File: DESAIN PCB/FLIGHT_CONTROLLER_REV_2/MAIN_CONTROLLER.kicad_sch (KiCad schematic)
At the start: 31 parts, among them J1 AVR-ISP-10, J2 USB B, J3 Conn_01x03_Male, J4 Conn_01x03_Male, J5 Conn_01x03_Male, J6 Conn_01x03_Male, J7 Conn_01x08_Female, J8 Conn_01x08_Female, SW1 SW_SPST, U1 ATmega328P-P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

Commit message: add PCB REV 2
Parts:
- added J12: TRANSMITTER_1, Connector_PinHeader_2.54mm:PinHeader_1x04_P2.54mm_Vertical, symbol Connector:Conn_01x04_Male
- added J13: TRANSMITTER_2, Connector_PinHeader_2.54mm:PinHeader_1x04_P2.54mm_Vertical, symbol Connector:Conn_01x04_Male
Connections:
- net MOSI is gone; now on net D11: J1.1 (MOSI), U1.17 (PB3)
- net +5V: now also J12.1 (Pin_1), J13.1 (Pin_1)
- net GND: now also J12.4 (Pin_4), J13.4 (Pin_4)
- net RX: now also J12.2 (Pin_2), J13.2 (Pin_2)
- net TX: now also J12.3 (Pin_3), J13.3 (Pin_3)
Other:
- note removed: "==> D11"
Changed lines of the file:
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@@
+    (stroke (width 0) (type default) (color 0 0 0 0))
+  )
+  (wire (pts (xy 132.08 127) (xy 137.16 127))
     (stroke (width 0) (type default) (color 0 0 0 0))
   )
@@
     (stroke (width 0) (type default) (color 0 0 0 0))
   )
+  (wire (pts (xy 152.4 127) (xy 157.48 127))
+    (stroke (width 0) (type default) (color 0 0 0 0))
+  )
   (polyline (pts (xy 153.67 101.092) (xy 153.67 112.776))
     (stroke (width 0) (type default) (color 0 0 0 0))
@@
     (stroke (width 0) (type default) (color 0 0 0 0))
   )
+  (wire (pts (xy 132.08 124.46) (xy 137.16 124.46))
+    (stroke (width 0) (type default) (color 0 0 0 0))
+  )
   (polyline (pts (xy 129.54 36.195) (xy 129.54 48.26))
     (stroke (width 0) (type default) (color 0 0 0 0))
@@
     (stroke (width 0) (type default) (color 0 0 0 0))
   )
+  (wire (pts (xy 56.896 43.18) (xy 74.93 43.18))
+    (stroke (width 0) (type default) (color 0 0 0 0))
+  )
   (polyline (pts (xy 18.542 113.792) (xy 18.542 115.062))
     (stroke (width 0) (type default) (color 0 0 0 0))
@@
     (stroke (width 0) (type default) (color 0 0 0 0))
   )
-  (wire (pts (xy 56.896 43.18) (xy 65.786 43.18))
-    (stroke (width 0) (type default) (color 0 0 0 0))
-  )
   (polyline (pts (xy 205.994 85.344) (xy 205.994 88.138))
     (stroke (width 0) (type default) (color 0 0 0 0))
   )
   (wire (pts (xy 130.81 34.925) (xy 130.81 44.958))
+    (stroke (width 0) (type default) (color 0 0 0 0))
+  )
+  (wire (pts (xy 152.4 124.46) (xy 157.48 124.46))
     (stroke (width 0) (type default) (color 0 0 0 0))
   )
@@
     (effects (font (size 1.27 1.27) (thickness 0.254) bold) (justify left bottom))
   )
-  (text "==> D11" (at 65.786 43.18 0)
-    (effects (font (size 1.27 1.27)) (justify left bottom))
-  )
   (text "IMU GY 88-A" (at 209.804 89.408 0)
     (effects (font (size 1.27 1.27) bold) (justify left bottom))
@@
     (effects (font (size 1.27 1.27)) (justify right bottom))
   )
+  (label "RX" (at 137.16 124.46 180)
+    (effects (font (size 1.27 1.27)) (justify right bottom))
+  )
   (label "D4" (at 65.786 88.9 180)
     (effects (font (size 1.27 1.27)) (justify right bottom))
@@
   )
   (label "D7" (at 174.498 108.204 180)
+    (effects (font (size 1.27 1.27)) (justify right bottom))
+  )
+  (label "TX" (at 157.48 127 180)
     (effects (font (size 1.27 1.27)) (justify right bottom))
   )
@@
     (effects (font (size 1.27 1.27)) (justify right bottom))
   )
+  (label "TX" (at 137.16 127 180)
+    (effects (font (size 1.27 1.27)) (justify right bottom))
+  )
   (label "D9" (at 149.098 98.044 180)
     (effects (font (size 1.27 1.27)) (justify right bottom))
@@
   )
   (label "D4" (at 174.498 100.584 180)
+    (effects (font (size 1.27 1.27)) (justify right bottom))
+  )
+  (label "RX" (at 157.48 124.46 180)
+    (effects (font (size 1.27 1.27)) (justify right bottom))
+  )
+  (label "D11" (at 74.93 43.18 180)
     (effects (font (size 1.27 1.27)) (justify right bottom))
   )
@@
     (pin "3")
   )
+  (symbol (lib_id "power:GND") (at 152.4 129.54 90) (unit 1)
+    (in_bom yes) (on_board yes) (fields_autoplaced)
+    (property "Reference" "#PWR0108" (id 0) (at 158.75 129.54 0)
+      (effects (font (size 1.27 1.27)) hide)
+    )
+    (property "Value" "GND" (id 1) (at 156.21 129.5399 90)
+      (effects (font (size 1.27 1.27)) (justify right))
+    )
+    (property "Footprint" "" (id 2) (at 152.4 129.54 0)
+      (effects (font (size 1.27 1.27)) hide)
+    )
+    (property "Datasheet" "" (id 3) (at 152.4 129.54 0)
+      (effects (font (size 1.27 1.27)) hide)
+    )
+    (pin "1")
+  )
   (symbol (lib_id "Device:C_Small") (at 94.742 45.974 270) (mirror x) (unit 1)
     (in_bom yes) (on_board yes)
@@
     (pin "8")
     (pin "9")
+  )
+  (symbol (lib_id "power:GND") (at 132.08 129.54 90) (unit 1)
+    (in_bom yes) (on_board yes) (fields_autoplaced)
+    (property "Reference" "#PWR0105" (id 0) (at 138.43 129.54 0)
+      (effects (font (size 1.27 1.27)) hide)
+    )
+    (property "Value" "GND" (id 1) (at 135.89 129.5399 90)
+      (effects (font (size 1.27 1.27)) (justify right))
+    )
+    (property "Footprint" "" (id 2) (at 132.08 129.54 0)
+      (effects (font (size 1.27 1.27)) hide)
+    )
+    (property "Datasheet" "" (id 3) (at 132.08 129.54 0)
+      (effects (font (size 1.27 1.27)) hide)
+    )
+    (pin "1")
   )
   (symbol (lib_id "Connector:Conn_01x03_Male") (at 141.224 94.996 0) (unit 1)
@@
     (pin "2")
   )
+  (symbol (lib_id "power:+5V") (at 152.4 121.92 270) (unit 1)
+    (in_bom yes) (on_board yes) (fields_autoplaced)
+    (property "Reference" "#PWR0107" (id 0) (at 148.59 121.92 0)
+      (effects (font (size 1.27 1.27)) hide)
+    )
+    (property "Value" "+5V" (id 1) (at 156.21 121.9199 90)
+      (effects (font (size 1.27 1.27)) (justify left))
+    )
+    (property "Footprint" "" (id 2) (at 152.4 121.92 0)
+      (effects (font (size 1.27 1.27)) hide)
+    )
+    (property "Datasheet" "" (id 3) (at 152.4 121.92 0)
+      (effects (font (size 1.27 1.27)) hide)
+    )
+    (pin "1")
+  )
   (symbol (lib_id "power:+5V") (at 131.064 94.996 270) (unit 1)
     (in_bom yes) (on_board yes)
@@
     (pin "2")
   )
+  (symbol (lib_id "Connector:Conn_01x04_Male") (at 147.32 124.46 0) (unit 1)
+    (in_bom yes) (on_board yes) (fields_autoplaced)
+    (property "Reference" "J13" (id 0) (at 147.955 116.84 0))
+    (property "Value" "TRANSMITTER_2" (id 1) (at 147.955 119.38 0))
+    (property "Footprint" "Connector_PinHeader_2.54mm:PinHeader_1x04_P2.54mm_Vertical" (id 2) (at 147.32 124.46 0)
+      (effects (font (size 1.27 1.27)) hide)
+    )
+    (property "Datasheet" "~" (id 3) (at 147.32 124.46 0)
+      (effects (font (size 1.27 1.27)) hide)
+    )
+    (pin "1")
+    (pin "2")
+    (pin "3")
+    (pin "4")
+  )
   (symbol (lib_id "Device:C_Small") (at 84.328 65.024 0) (unit 1)
     (in_bom yes) (on_board yes)
@@
     (pin "1")
     (pin "2")
+  )
+  (symbol (lib_id "power:+5V") (at 132.08 121.92 270) (unit 1)
+    (in_bom yes) (on_board yes) (fields_autoplaced)
+    (property "Reference" "#PWR0106" (id 0) (at 128.27 121.92 0)
+      (effects (font (size 1.27 1.27)) hide)
+    )
+    (property "Value" "+5V" (id 1) (at 135.89 121.9199 90)
+      (effects (font (size 1.27 1.27)) (justify left))
+    )
+    (property "Footprint" "" (id 2) (at 132.08 121.92 0)
+      (effects (font (size 1.27 1.27)) hide)
+    )
+    (property "Datasheet" "" (id 3) (at 132.08 121.92 0)
+      (effects (font (size 1.27 1.27)) hide)
+    )
+    (pin "1")
   )
   (symbol (lib_id "power:GND") (at 102.108 45.974 0) (mirror y) (unit 1)
@@
     (pin "1")
   )
+  (symbol (lib_id "Connector:Conn_01x04_Male") (at 127 124.46 0) (unit 1)
+    (in_bom yes) (on_board yes) (fields_autoplaced)
+    (property "Reference" "J12" (id 0) (at 127.635 116.84 0))
+    (property "Value" "TRANSMITTER_1" (id 1) (at 127.635 119.38 0))
+    (property "Footprint" "Connector_PinHeader_2.54mm:PinHeader_1x04_P2.54mm_Vertical" (id 2) (at 127 124.46 0)
+      (effects (font (size 1.27 1.27)) hide)
+    )
+    (property "Datasheet" "~" (id 3) (at 127 124.46 0)
+      (effects (font (size 1.27 1.27)) hide)
+    )
+    (pin "1")
+    (pin "2")
+    (pin "3")
+    (pin "4")
+  )
 )

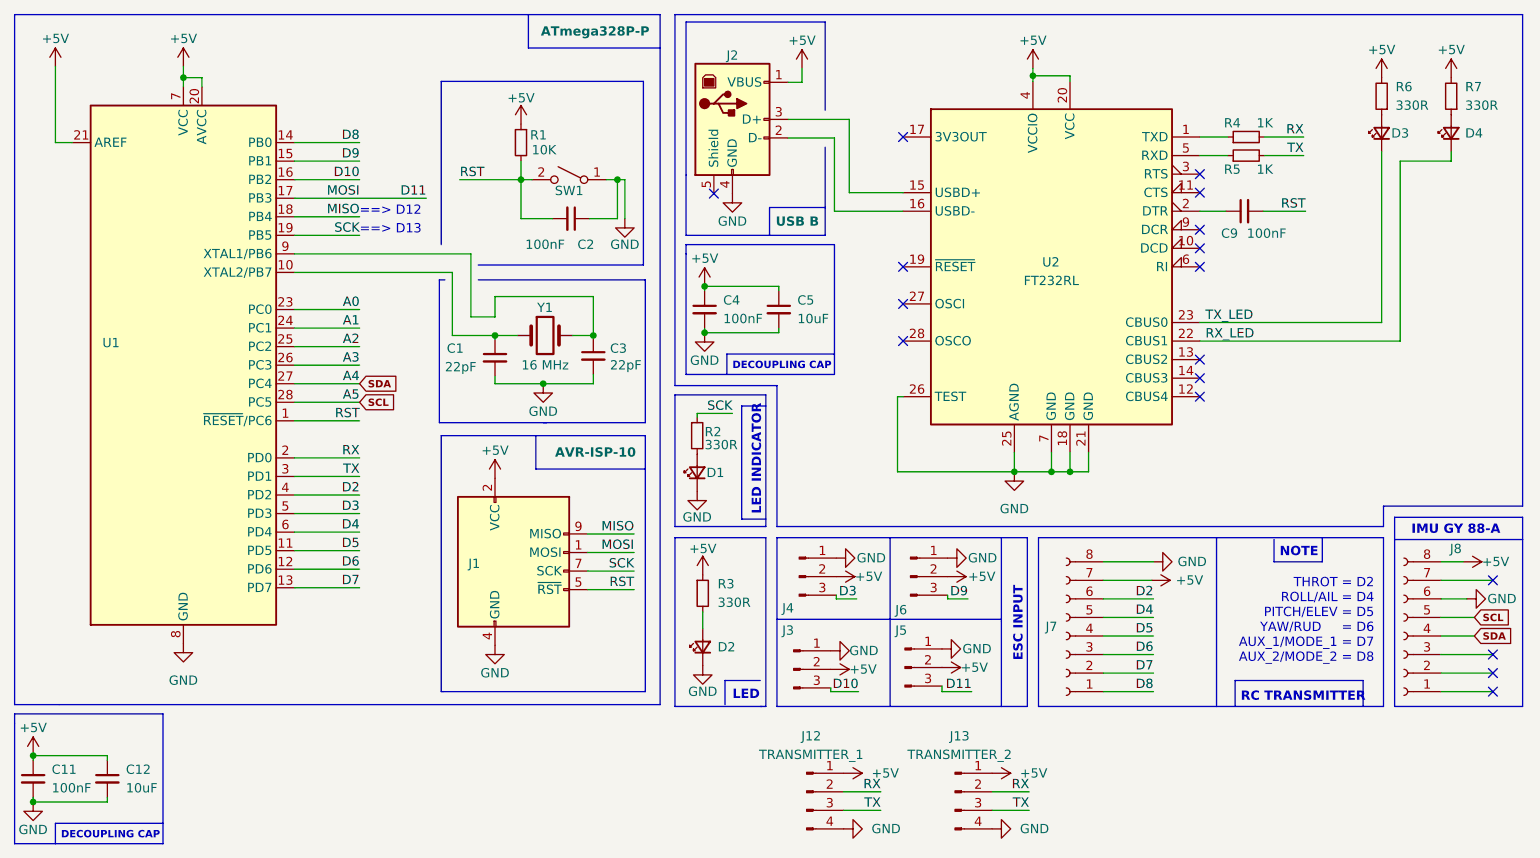
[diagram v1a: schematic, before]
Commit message: add new files
- more documentation files for PCB Rev 2
- add PCB Rev 3
- add 3D Models
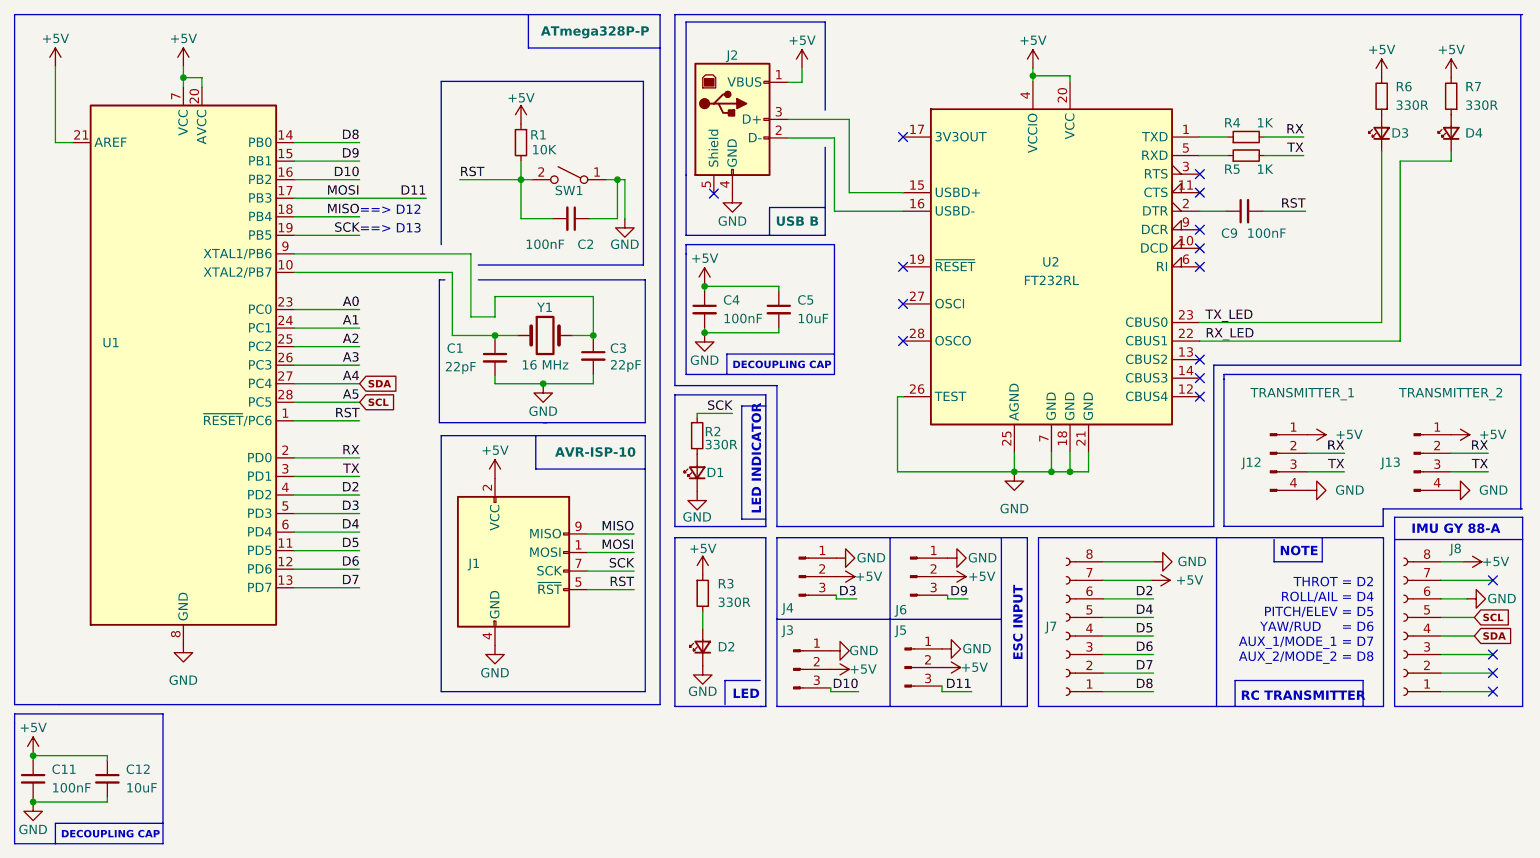
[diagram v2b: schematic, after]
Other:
- moved on the sheet: J12, J13
